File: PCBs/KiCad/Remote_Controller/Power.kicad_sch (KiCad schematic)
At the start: 26 parts

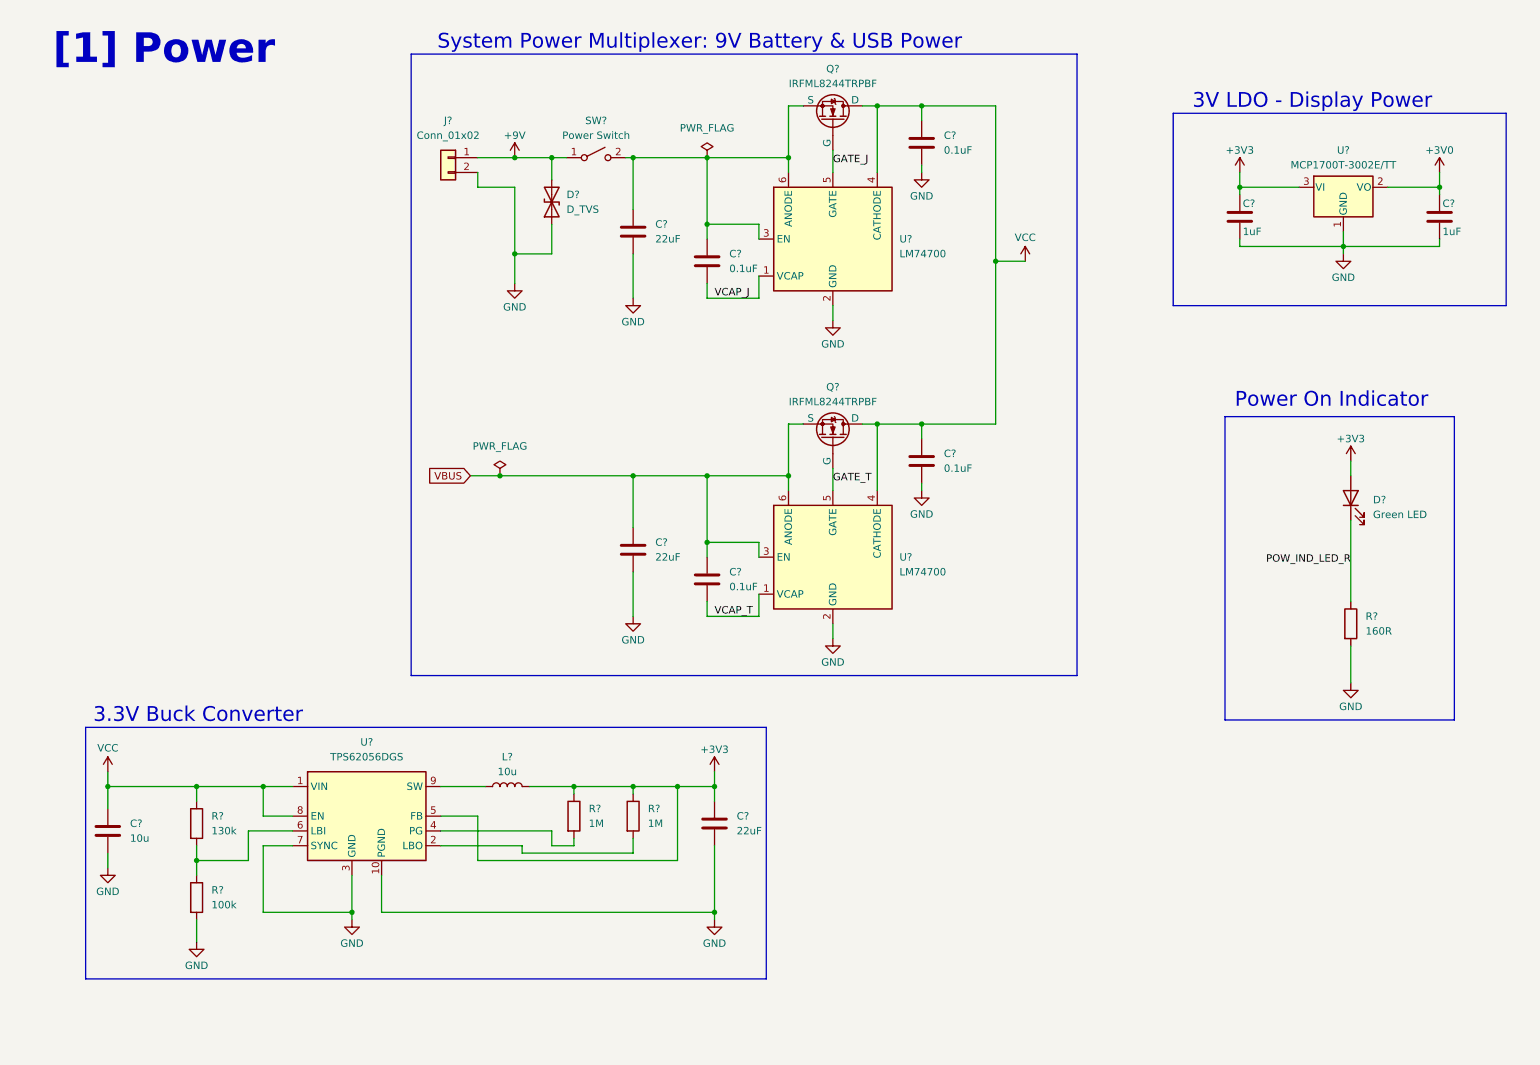
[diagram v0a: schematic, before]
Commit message: Labeled all nets, corrected some labels, added battery-cell symbol
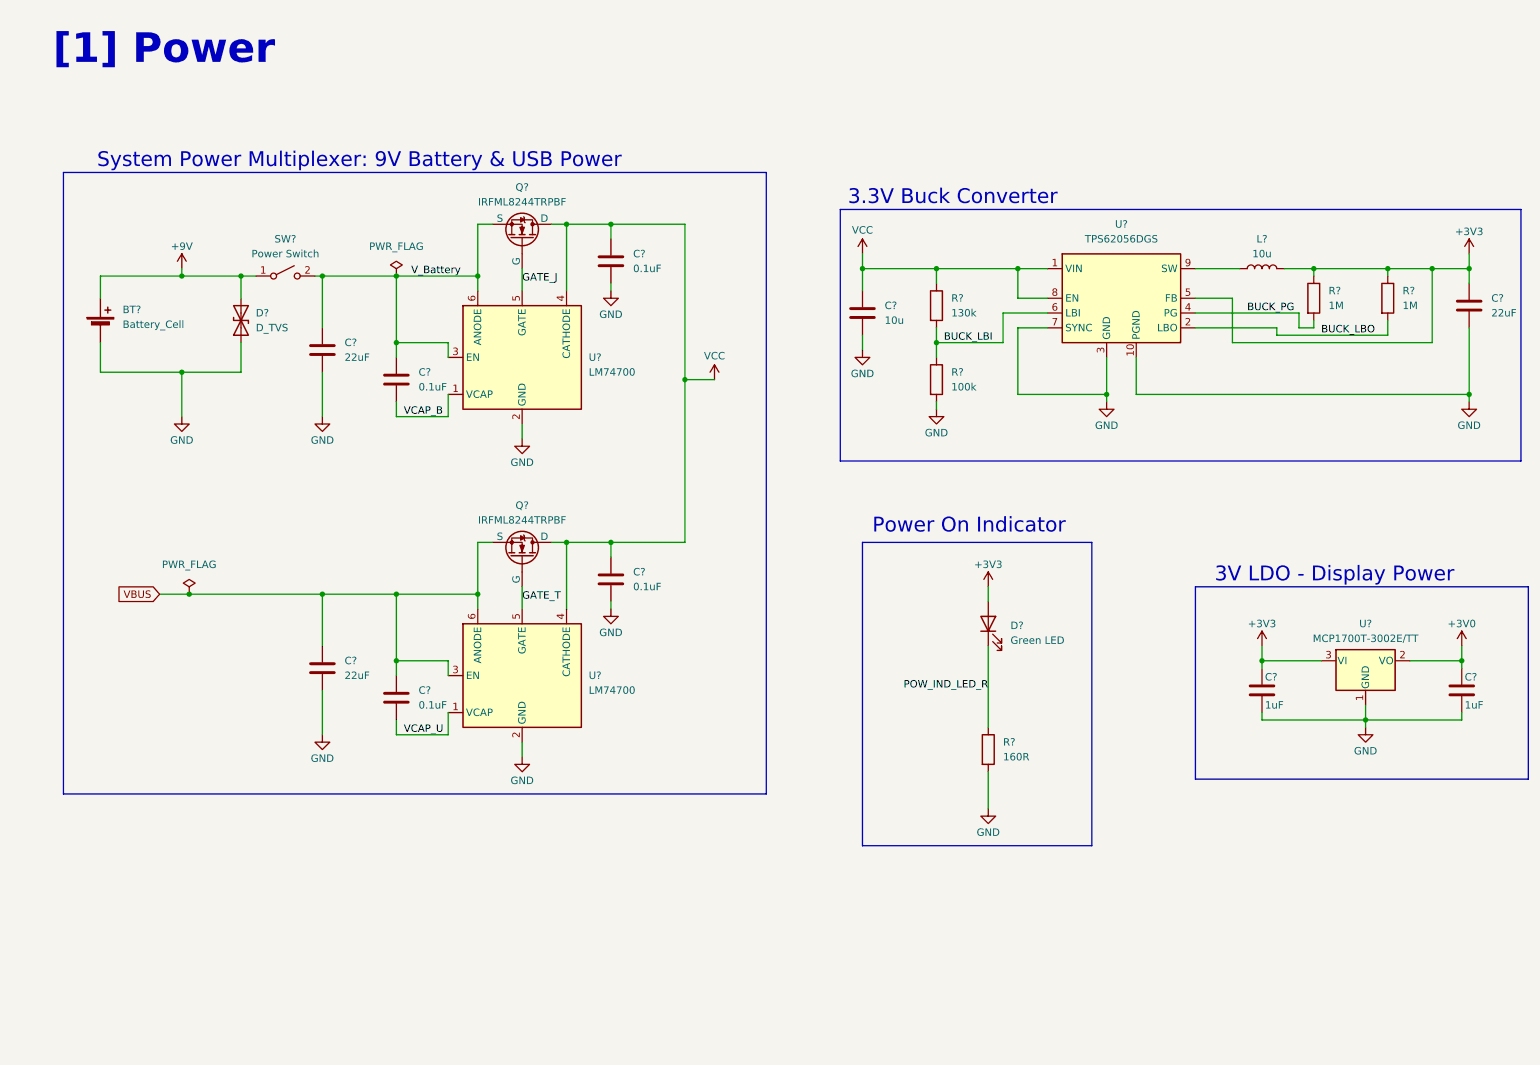
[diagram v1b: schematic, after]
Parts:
- removed J?: Conn_01x02, symbol Connector_Generic:Conn_01x02
- added BT?: Battery_Cell, symbol Device:Battery_Cell
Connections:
- net +9V: now also BT?.1 (+)
- net GND: now also BT?.2 (-)
- net V_Battery: now reaches C?.1, C?.1, Q?.2 (S), SW?.2 (B), U?.3 (EN), U?.6 (ANODE)
- net BUCK_LBO: now reaches R?.2, U?.2 (LBO)
- net BUCK_PG: now reaches R?.2, U?.4 (PG)
- net BUCK_LBI: now reaches R?.1, R?.2, U?.6 (LBI)
- net VCAP_J renamed VCAP_B
- net VCAP_T renamed VCAP_U
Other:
- moved on the sheet: C?, D?, L?, Q?, R?, SW?, U?

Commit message: Added Buck converter with a reverse breakdown voltage that is much higher than the nominal input voltage, and added TVS diode
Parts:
- removed C?: 22uF, symbol Device:C
- removed C?: 10u, symbol Device:C
- removed L?: 10u, symbol Device:L
- removed R?: 100k, symbol Device:R
- removed R? (x2): 1M, symbol Device:R
- removed R?: 130k, symbol Device:R
- removed U?: TPS62056DGS, Package_SO:VSSOP-10_3x3mm_P0.5mm, symbol Regulator_Switching:TPS62056DGS
- added C?: 10uF, symbol Device:C
- added C? (x2): 22uF, symbol Device:C
- added C?: 0.1uF, symbol Device:C
- added L?: 3.9uF, symbol Device:L
- added U?: AP63203WU, Package_TO_SOT_SMD:TSOT-23-6, symbol Regulator_Switching:AP63203WU
- D?: value D_TVS -> P6SMB22CA
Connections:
- net +3V3: now also C?.1, C?.1, L?.2, U?.1 (FB)
- net GND: now also C?.2, C?.2, C?.2, U?.4 (GND)
- net VCC: now also C?.1, U?.2 (EN), U?.3 (IN)
- net GATE_J renamed GATE_B
- net GATE_T renamed GATE_U
- new net BUCK_BST: C?.2, U?.6 (BST)
- new net BUCK_SW: C?.1, L?.1, U?.5 (SW)
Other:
- moved on the sheet: D?

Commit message: Annotate components
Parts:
- gave numbers to parts that had none: 24
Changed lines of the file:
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@@
 		(dnp no)
 		(fields_autoplaced yes)
-		(property "Reference" "C?"
+		(property "Reference" "C108"
 			(at 116.84 111.7599 0)
 			(effects
@@
 			(project "Remote_Controller"
 				(path "/7afb5074-6b77-4607-a5eb-938c2def45ba/bc757f9b-317d-459c-8896-b31b23ed4983"
-					(reference "C?")
+					(reference "C108")
 					(unit 1)
 				)
@@
 		(dnp no)
 		(fields_autoplaced yes)
-		(property "Reference" "C?"
+		(property "Reference" "C104"
 			(at 67.31 72.3899 0)
 			(effects
@@
 			(project "Remote_Controller"
 				(path "/7afb5074-6b77-4607-a5eb-938c2def45ba/bc757f9b-317d-459c-8896-b31b23ed4983"
-					(reference "C?")
+					(reference "C104")
 					(unit 1)
 				)
@@
 		(dnp no)
 		(fields_autoplaced yes)
-		(property "Reference" "C?"
+		(property "Reference" "C109"
 			(at 67.31 126.9999 0)
 			(effects
@@
 			(project "Remote_Controller"
 				(path "/7afb5074-6b77-4607-a5eb-938c2def45ba/bc757f9b-317d-459c-8896-b31b23ed4983"
-					(reference "C?")
+					(reference "C109")
 					(unit 1)
 				)
@@
 		(on_board yes)
 		(dnp no)
-		(property "Reference" "Q?"
+		(property "Reference" "Q102"
 			(at 97.79 100.33 90)
 			(effects
@@
 			(project "Remote_Controller"
 				(path "/7afb5074-6b77-4607-a5eb-938c2def45ba/bc757f9b-317d-459c-8896-b31b23ed4983"
-					(reference "Q?")
+					(reference "Q102")
 					(unit 1)
 				)
@@
 		(dnp no)
 		(fields_autoplaced yes)
-		(property "Reference" "L?"
+		(property "Reference" "L101"
 			(at 227.33 54.61 90)
 			(effects
@@
 			(project ""
 				(path "/7afb5074-6b77-4607-a5eb-938c2def45ba/bc757f9b-317d-459c-8896-b31b23ed4983"
-					(reference "L?")
+					(reference "L101")
 					(unit 1)
 				)
@@
 		(dnp no)
 		(fields_autoplaced yes)
-		(property "Reference" "C?"
+		(property "Reference" "C101"
 			(at 116.84 57.1499 0)
 			(effects
@@
 			(project "Remote_Controller"
 				(path "/7afb5074-6b77-4607-a5eb-938c2def45ba/bc757f9b-317d-459c-8896-b31b23ed4983"
-					(reference "C?")
+					(reference "C101")
 					(unit 1)
 				)
@@
 		(dnp no)
 		(fields_autoplaced yes)
-		(property "Reference" "C?"
+		(property "Reference" "C107"
 			(at 80.01 77.4699 0)
 			(effects
@@
 			(project "Remote_Controller"
 				(path "/7afb5074-6b77-4607-a5eb-938c2def45ba/bc757f9b-317d-459c-8896-b31b23ed4983"
-					(reference "C?")
+					(reference "C107")
 					(unit 1)
 				)
@@
 		(dnp no)
 		(fields_autoplaced yes)
-		(property "Reference" "C?"
+		(property "Reference" "C112"
 			(at 80.01 132.0799 0)
 			(effects
@@
 			(project "Remote_Controller"
 				(path "/7afb5074-6b77-4607-a5eb-938c2def45ba/bc757f9b-317d-459c-8896-b31b23ed4983"
-					(reference "C?")
+					(reference "C112")
 					(unit 1)
 				)
@@
 		(dnp no)
 		(fields_autoplaced yes)
-		(property "Reference" "BT?"
+		(property "Reference" "BT101"
 			(at 29.21 66.7384 0)
 			(effects
@@
 			(project ""
 				(path "/7afb5074-6b77-4607-a5eb-938c2def45ba/bc757f9b-317d-459c-8896-b31b23ed4983"
-					(reference "BT?")
+					(reference "BT101")
 					(unit 1)
 				)
@@
 		(dnp no)
 		(fields_autoplaced yes)
-		(property "Reference" "D?"
+		(property "Reference" "D102"
 			(at 181.61 120.9674 90)
 			(effects
@@
 			(project "Remote_Controller"
 				(path "/7afb5074-6b77-4607-a5eb-938c2def45ba/bc757f9b-317d-459c-8896-b31b23ed4983"
-					(reference "D?")
+					(reference "D102")
 					(unit 1)
 				)
@@
 		(dnp no)
 		(fields_autoplaced yes)
-		(property "Reference" "U?"
+		(property "Reference" "U101"
 			(at 198.12 59.69 0)
 			(effects
@@
 			(project ""
 				(path "/7afb5074-6b77-4607-a5eb-938c2def45ba/bc757f9b-317d-459c-8896-b31b23ed4983"
-					(reference "U?")
+					(reference "U101")
 					(unit 1)
 				)
@@
 		(on_board yes)
 		(dnp no)
-		(property "Reference" "Q?"
+		(property "Reference" "Q101"
 			(at 97.79 45.72 90)
 			(effects
@@
 			(project "Remote_Controller"
 				(path "/7afb5074-6b77-4607-a5eb-938c2def45ba/bc757f9b-317d-459c-8896-b31b23ed4983"
-					(reference "Q?")
+					(reference "Q101")
 					(unit 1)
 				)
@@
 		(dnp no)
 		(fields_autoplaced yes)
-		(property "Reference" "U?"
+		(property "Reference" "U104"
 			(at 109.22 129.5399 0)
 			(effects
@@
 			(project "Remote_Controller"
 				(path "/7afb5074-6b77-4607-a5eb-938c2def45ba/bc757f9b-317d-459c-8896-b31b23ed4983"
-					(reference "U?")
+					(reference "U104")
 					(unit 1)
 				)
@@
 		(on_board yes)
 		(dnp no)
-		(property "Reference" "C?"
+		(property "Reference" "C111"
 			(at 259.588 129.794 0)
 			(effects
@@
 			(project "Remote_Controller"
 				(path "/7afb5074-6b77-4607-a5eb-938c2def45ba/bc757f9b-317d-459c-8896-b31b23ed4983"
-					(reference "C?")
+					(reference "C111")
 					(unit 1)
 				)
@@
 		(dnp no)
 		(fields_autoplaced yes)
-		(property "Reference" "U?"
+		(property "Reference" "U103"
 			(at 242.57 120.65 0)
 			(effects
@@
 			(project "Remote_Controller"
 				(path "/7afb5074-6b77-4607-a5eb-938c2def45ba/bc757f9b-317d-459c-8896-b31b23ed4983"
-					(reference "U?")
+					(reference "U103")
 					(unit 1)
 				)
@@
 		(dnp no)
 		(fields_autoplaced yes)
-		(property "Reference" "C?"
+		(property "Reference" "C103"
 			(at 177.8 71.1199 0)
 			(effects
@@
 			(project ""
 				(path "/7afb5074-6b77-4607-a5eb-938c2def45ba/bc757f9b-317d-459c-8896-b31b23ed4983"
-					(reference "C?")
+					(reference "C103")
 					(unit 1)
 				)
@@
 		(dnp no)
 		(fields_autoplaced yes)
-		(property "Reference" "C?"
+		(property "Reference" "C106"
 			(at 250.19 72.3899 0)
 			(effects
@@
 			(project "Remote_Controller"
 				(path "/7afb5074-6b77-4607-a5eb-938c2def45ba/bc757f9b-317d-459c-8896-b31b23ed4983"
-					(reference "C?")
+					(reference "C106")
 					(unit 1)
 				)
@@
 		(dnp no)
 		(fields_autoplaced yes)
-		(property "Reference" "SW?"
+		(property "Reference" "SW101"
 			(at 57.15 54.61 0)
 			(effects
@@
 			(project ""
 				(path "/7afb5074-6b77-4607-a5eb-938c2def45ba/bc757f9b-317d-459c-8896-b31b23ed4983"
-					(reference "SW?")
+					(reference "SW101")
 					(unit 1)
 				)
@@
 		(dnp no)
 		(fields_autoplaced yes)
-		(property "Reference" "C?"
+		(property "Reference" "C102"
 			(at 223.52 63.4999 0)
 			(effects
@@
 			(project "Remote_Controller"
 				(path "/7afb5074-6b77-4607-a5eb-938c2def45ba/bc757f9b-317d-459c-8896-b31b23ed4983"
-					(reference "C?")
+					(reference "C102")
 					(unit 1)
 				)
@@
 		(on_board yes)
 		(dnp no)
-		(property "Reference" "C?"
+		(property "Reference" "C110"
 			(at 225.298 129.794 0)
 			(effects
@@
 			(project "Remote_Controller"
 				(path "/7afb5074-6b77-4607-a5eb-938c2def45ba/bc757f9b-317d-459c-8896-b31b23ed4983"
-					(reference "C?")
+					(reference "C110")
 					(unit 1)
 				)
@@
 		(dnp no)
 		(fields_autoplaced yes)
-		(property "Reference" "C?"
+		(property "Reference" "C105"
 			(at 237.49 72.3899 0)
 			(effects
@@
 			(project "Remote_Controller"
 				(path "/7afb5074-6b77-4607-a5eb-938c2def45ba/bc757f9b-317d-459c-8896-b31b23ed4983"
-					(reference "C?")
+					(reference "C105")
 					(unit 1)
 				)
@@
 		(dnp no)
 		(fields_autoplaced yes)
-		(property "Reference" "U?"
+		(property "Reference" "U102"
 			(at 109.22 74.9299 0)
 			(effects
@@
 			(project "Remote_Controller"
 				(path "/7afb5074-6b77-4607-a5eb-938c2def45ba/bc757f9b-317d-459c-8896-b31b23ed4983"
-					(reference "U?")
+					(reference "U102")
 					(unit 1)
 				)
@@
 		(dnp no)
 		(fields_autoplaced yes)
-		(property "Reference" "R?"
+		(property "Reference" "R101"
 			(at 180.34 140.9699 0)
 			(effects
@@
 			(project "Remote_Controller"
 				(path "/7afb5074-6b77-4607-a5eb-938c2def45ba/bc757f9b-317d-459c-8896-b31b23ed4983"
-					(reference "R?")
+					(reference "R101")
 					(unit 1)
 				)
@@
 		(dnp no)
 		(fields_autoplaced yes)
-		(property "Reference" "D?"
+		(property "Reference" "D101"
 			(at 49.53 67.3099 90)
 			(effects
@@
 			(project "Remote_Controller"
 				(path "/7afb5074-6b77-4607-a5eb-938c2def45ba/bc757f9b-317d-459c-8896-b31b23ed4983"
-					(reference "D?")
-					(unit 1)
-				)
+					(reference "D101")
+					(unit 1)
+				)

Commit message: Add footprints except connectors, buttons and switches
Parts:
- BT101: footprint (none) -> Battery:BatteryHolder_MPD_BA9VPC_1xPP3
- C102: footprint (none) -> Capacitor_SMD:C_0402_1005Metric
- C103: footprint (none) -> Capacitor_SMD:C_0805_2012Metric
- C105, C106: footprint (none) -> Capacitor_SMD:C_1206_3216Metric
- L101: footprint (none) -> Inductor_SMD:L_Vishay_IHLP-2525
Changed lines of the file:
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@@
 			)
 		)
-		(property "Footprint" ""
+		(property "Footprint" "Inductor_SMD:L_Vishay_IHLP-2525"
 			(at 227.33 59.69 0)
 			(effects
@@
 			)
 		)
-		(property "Footprint" ""
+		(property "Footprint" "Battery:BatteryHolder_MPD_BA9VPC_1xPP3"
 			(at 25.4 68.326 90)
 			(effects
@@
 			)
 		)
-		(property "Footprint" ""
+		(property "Footprint" "Capacitor_SMD:C_0805_2012Metric"
 			(at 174.9552 76.2 0)
 			(effects
@@
 			)
 		)
-		(property "Footprint" ""
+		(property "Footprint" "Capacitor_SMD:C_1206_3216Metric"
 			(at 247.3452 77.47 0)
 			(effects
@@
 			)
 		)
-		(property "Footprint" ""
+		(property "Footprint" "Capacitor_SMD:C_0402_1005Metric"
 			(at 220.6752 68.58 0)
 			(effects
@@
 			)
 		)
-		(property "Footprint" ""
+		(property "Footprint" "Capacitor_SMD:C_1206_3216Metric"
 			(at 234.6452 77.47 0)
 			(effects
